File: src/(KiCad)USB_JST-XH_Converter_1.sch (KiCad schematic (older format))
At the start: 25 parts, among them SW1 SS-12D00G3, U2 TLP293

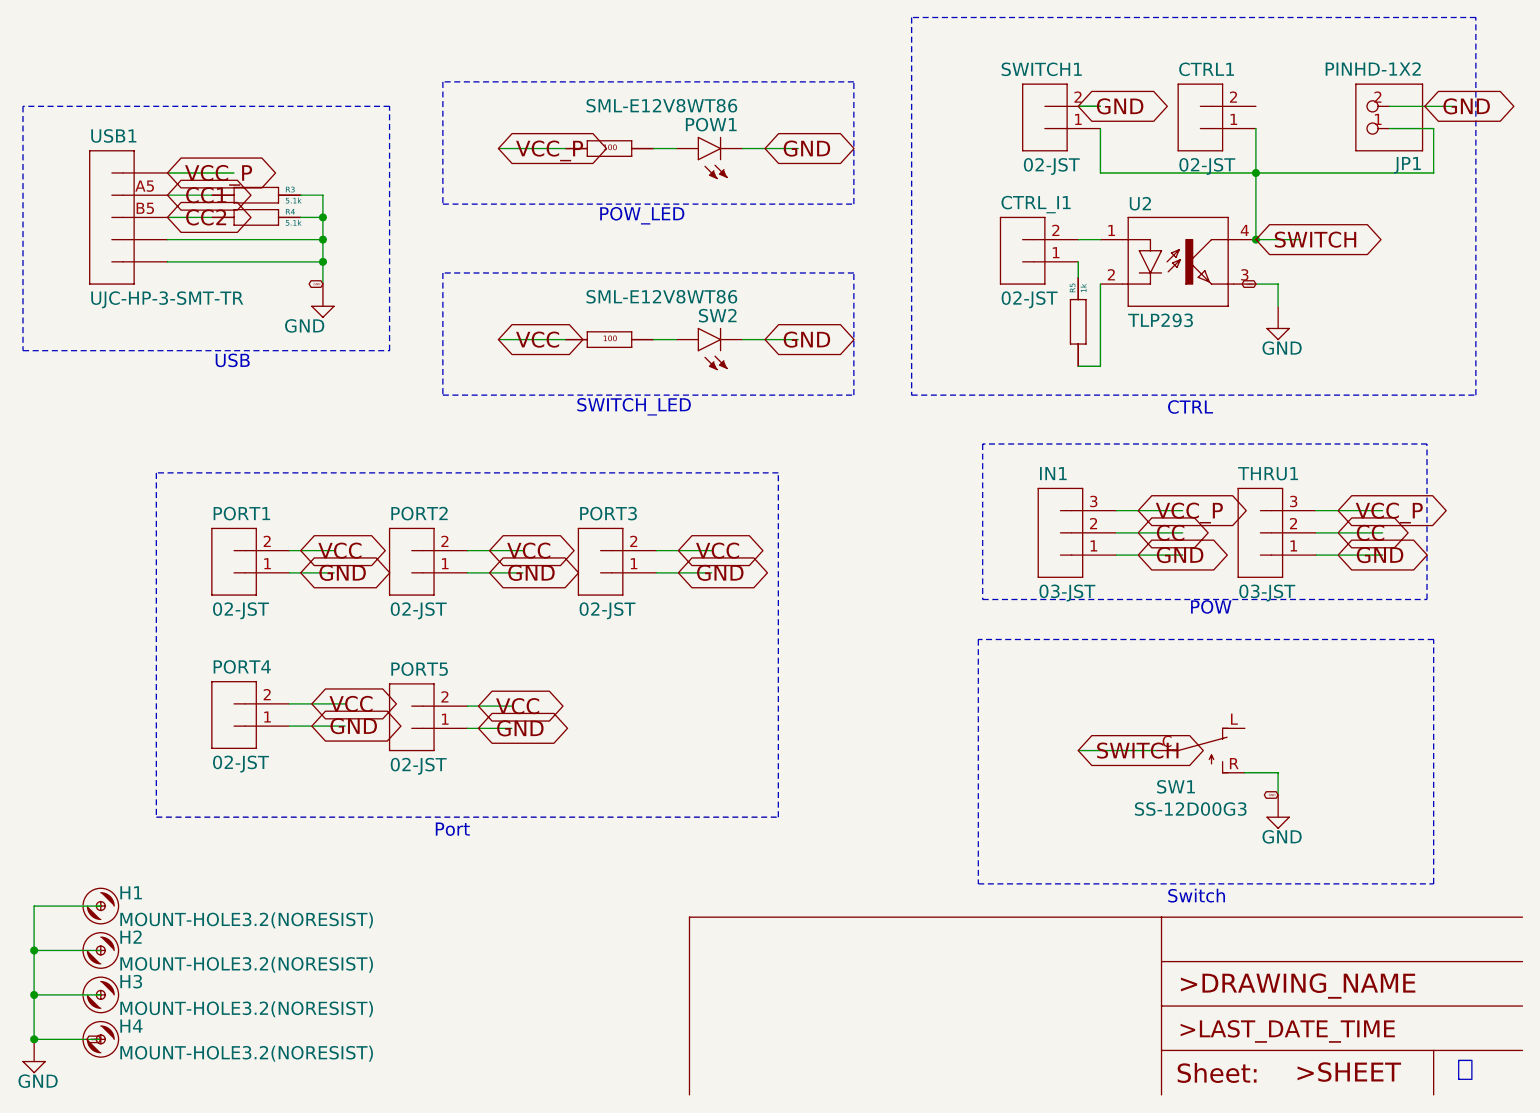
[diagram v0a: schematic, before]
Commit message: 3Aモード用LEDの追加
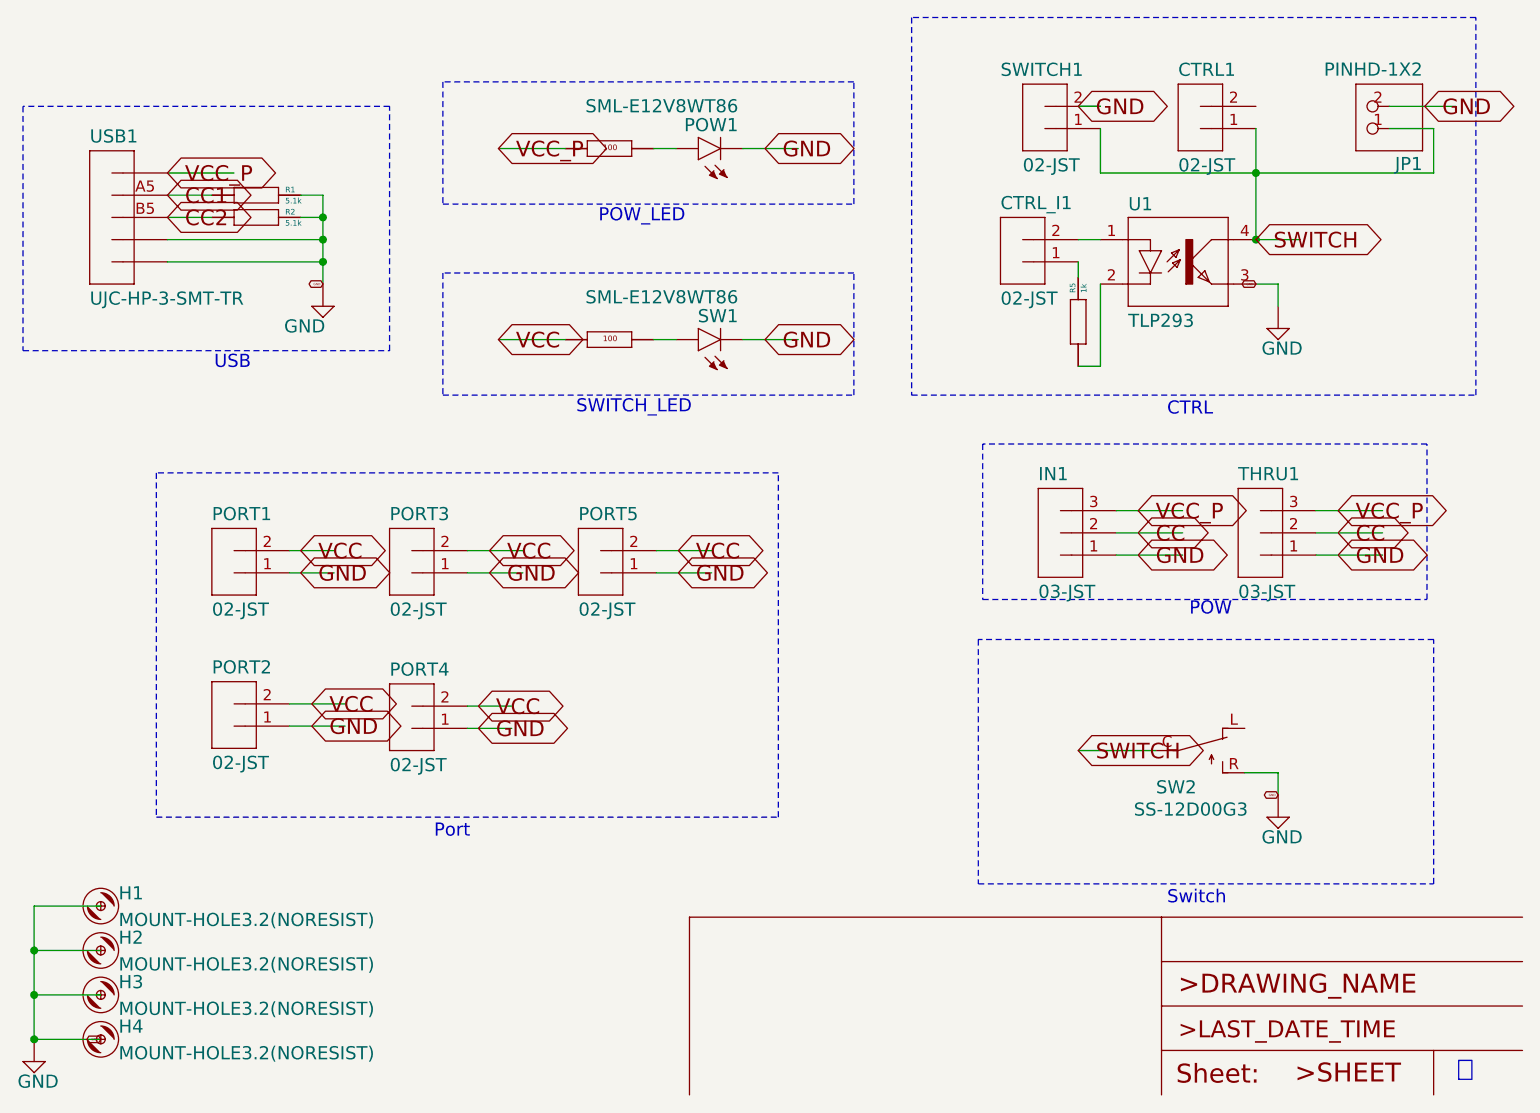
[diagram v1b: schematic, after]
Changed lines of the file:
@@
 AR Path="/CC96BE83" Ref="#FRAME1"  Part="1"
 AR Path="/639B4B9A/CC96BE83" Ref="#FRAME1"  Part="1"
+AR Path="/639EA9E5/CC96BE83" Ref="#FRAME1"  Part="1"
 F 0 "#FRAME1" H 2300 6600 50  0001 C CNN
 F 1 "A5L-LOC" H 2300 6600 50  0001 C CNN
@@
 AR Path="/96A0C2AF" Ref="PORT1"  Part="1"
 AR Path="/639B4B9A/96A0C2AF" Ref="PORT1"  Part="1"
+AR Path="/639EA9E5/96A0C2AF" Ref="PORT1"  Part="1"
 F 0 "PORT1" H 3500 4130 59  0000 L BNN
 F 1 "02-JST" H 3500 3700 59  0000 L BNN
@@
 AR Path="/DE65265B" Ref="PORT2"  Part="1"
 AR Path="/639B4B9A/DE65265B" Ref="PORT2"  Part="1"
-F 0 "PORT2" H 4300 4130 59  0000 L BNN
+AR Path="/639EA9E5/DE65265B" Ref="PORT3"  Part="1"
+F 0 "PORT3" H 4300 4130 59  0000 L BNN
 F 1 "02-JST" H 4300 3700 59  0000 L BNN
 F 2 "USB_JST-XH_Converter:B2B-XH" H 4350 4000 50  0001 C CNN
@@
 AR Path="/AF48B7E8" Ref="PORT3"  Part="1"
 AR Path="/639B4B9A/AF48B7E8" Ref="PORT3"  Part="1"
-F 0 "PORT3" H 5150 4130 59  0000 L BNN
+AR Path="/639EA9E5/AF48B7E8" Ref="PORT5"  Part="1"
+F 0 "PORT5" H 5150 4130 59  0000 L BNN
 F 1 "02-JST" H 5150 3700 59  0000 L BNN
 F 2 "USB_JST-XH_Converter:B2B-XH" H 5200 4000 50  0001 C CNN
@@
 AR Path="/423DE5BD" Ref="PORT4"  Part="1"
 AR Path="/639B4B9A/423DE5BD" Ref="PORT4"  Part="1"
-F 0 "PORT4" H 3500 4820 59  0000 L BNN
+AR Path="/639EA9E5/423DE5BD" Ref="PORT2"  Part="1"
+F 0 "PORT2" H 3500 4820 59  0000 L BNN
 F 1 "02-JST" H 3500 4390 59  0000 L BNN
 F 2 "USB_JST-XH_Converter:B2B-XH" H 3550 4690 50  0001 C CNN
@@
 AR Path="/35EB9426" Ref="PORT5"  Part="1"
 AR Path="/639B4B9A/35EB9426" Ref="PORT5"  Part="1"
-F 0 "PORT5" H 4300 4830 59  0000 L BNN
+AR Path="/639EA9E5/35EB9426" Ref="PORT4"  Part="1"
+F 0 "PORT4" H 4300 4830 59  0000 L BNN
 F 1 "02-JST" H 4300 4400 59  0000 L BNN
 F 2 "USB_JST-XH_Converter:B2B-XH" H 4350 4700 50  0001 C CNN
@@
 AR Path="/F85A3293" Ref="SW1"  Part="1"
 AR Path="/639B4B9A/F85A3293" Ref="SW1"  Part="1"
-F 0 "SW1" V 8150 4700 59  0000 L BNN
+AR Path="/639EA9E5/F85A3293" Ref="SW2"  Part="1"
+F 0 "SW2" V 8150 4700 59  0000 L BNN
 F 1 "SS-12D00G3" V 8250 4600 59  0000 L BNN
 F 2 "USB_JST-XH_Converter:SS-12D00G3" H 7950 4900 50  0001 C CNN
@@
 AR Path="/F54A36B8" Ref="#SUPPLY1"  Part="1"
 AR Path="/639B4B9A/F54A36B8" Ref="#SUPPLY01"  Part="1"
-F 0 "#SUPPLY01" H 8300 5200 50  0001 C CNN
+AR Path="/639EA9E5/F54A36B8" Ref="#SUPPLY0101"  Part="1"
+F 0 "#SUPPLY0101" H 8300 5200 50  0001 C CNN
 F 1 "GND" H 8225 5075 59  0000 L BNN
 F 2 "" H 8300 5200 50  0001 C CNN
@@
 AR Path="/5CC1AECC" Ref="SW"  Part="1"
 AR Path="/639B4B9A/5CC1AECC" Ref="SW2"  Part="1"
-F 0 "SW2" V 5830 2870 59  0000 L BNN
+AR Path="/639EA9E5/5CC1AECC" Ref="SW1"  Part="1"
+F 0 "SW1" V 5830 2870 59  0000 L BNN
 F 1 "SML-E12V8WT86" V 5915 2870 59  0000 L BNN
 F 2 "USB_JST-XH_Converter:SML-E12V8WT86" H 5690 3050 50  0001 C CNN
@@
 AR Path="/855FDFDB" Ref="R2"  Part="1"
 AR Path="/639B4B9A/855FDFDB" Ref="R2"  Part="1"
-F 0 "R2" H 5290 3050 50  0001 C CNN
+AR Path="/639EA9E5/855FDFDB" Ref="R4"  Part="1"
+F 0 "R4" H 5290 3050 50  0001 C CNN
 F 1 "RG2012N-101-B-T5" H 5290 3050 50  0001 C CNN
 F 2 "USB_JST-XH_Converter:RG2012" H 5290 3050 50  0001 C CNN
@@
 AR Path="/19032892" Ref="#SUPPLY2"  Part="1"
 AR Path="/639B4B9A/19032892" Ref="#SUPPLY02"  Part="1"
-F 0 "#SUPPLY02" H 2700 6300 50  0001 C CNN
+AR Path="/639EA9E5/19032892" Ref="#SUPPLY0102"  Part="1"
+F 0 "#SUPPLY0102" H 2700 6300 50  0001 C CNN
 F 1 "GND" H 2625 6175 59  0000 L BNN
 F 2 "" H 2700 6300 50  0001 C CNN
@@
 AR Path="/9910BFD8" Ref="H1"  Part="1"
 AR Path="/639B4B9A/9910BFD8" Ref="H1"  Part="1"
+AR Path="/639EA9E5/9910BFD8" Ref="H1"  Part="1"
 F 0 "H1" H 3080 5623 59  0000 L BNN
 F 1 "MOUNT-HOLE3.2(NORESIST)" H 3080 5503 59  0000 L BNN
@@
 AR Path="/5D268E00" Ref="H2"  Part="1"
 AR Path="/639B4B9A/5D268E00" Ref="H2"  Part="1"
+AR Path="/639EA9E5/5D268E00" Ref="H2"  Part="1"
 F 0 "H2" H 3080 5823 59  0000 L BNN
 F 1 "MOUNT-HOLE3.2(NORESIST)" H 3080 5703 59  0000 L BNN
@@
 AR Path="/DE67D20D" Ref="H3"  Part="1"
 AR Path="/639B4B9A/DE67D20D" Ref="H3"  Part="1"
+AR Path="/639EA9E5/DE67D20D" Ref="H3"  Part="1"
 F 0 "H3" H 3080 6023 59  0000 L BNN
 F 1 "MOUNT-HOLE3.2(NORESIST)" H 3080 5903 59  0000 L BNN
@@
 AR Path="/EA162BAB" Ref="H4"  Part="1"
 AR Path="/639B4B9A/EA162BAB" Ref="H4"  Part="1"
+AR Path="/639EA9E5/EA162BAB" Ref="H4"  Part="1"
 F 0 "H4" H 3080 6223 59  0000 L BNN
 F 1 "MOUNT-HOLE3.2(NORESIST)" H 3080 6103 59  0000 L BNN
@@
 AR Path="/4F8E092B" Ref="#SUPPLY3"  Part="1"
 AR Path="/639B4B9A/4F8E092B" Ref="#SUPPLY03"  Part="1"
-F 0 "#SUPPLY03" H 4000 2900 50  0001 C CNN
+AR Path="/639EA9E5/4F8E092B" Ref="#SUPPLY0103"  Part="1"
+F 0 "#SUPPLY0103" H 4000 2900 50  0001 C CNN
 F 1 "GND" H 3825 2775 59  0000 L BNN
 F 2 "" H 4000 2900 50  0001 C CNN
@@
 AR Path="/9A4BB1DE" Ref="R3"  Part="1"
 AR Path="/639B4B9A/9A4BB1DE" Ref="R3"  Part="1"
-F 0 "R3" H 3830 2410 25  0000 L BNN
+AR Path="/639EA9E5/9A4BB1DE" Ref="R1"  Part="1"
+F 0 "R1" H 3830 2410 25  0000 L BNN
 F 1 "5.1k" H 3830 2360 25  0000 L BNN
 F 2 "USB_JST-XH_Converter:RG2012" H 3700 2400 50  0001 C CNN
@@
 AR Path="/80DF3A02" Ref="R4"  Part="1"
 AR Path="/639B4B9A/80DF3A02" Ref="R4"  Part="1"
-F 0 "R4" H 3830 2510 25  0000 L BNN
+AR Path="/639EA9E5/80DF3A02" Ref="R2"  Part="1"
+F 0 "R2" H 3830 2510 25  0000 L BNN
 F 1 "5.1k" H 3830 2460 25  0000 L BNN
 F 2 "USB_JST-XH_Converter:RG2012" H 3700 2500 50  0001 C CNN
@@
 AR Path="/BF4A4BA7" Ref="SWITCH"  Part="1"
 AR Path="/639B4B9A/BF4A4BA7" Ref="SWITCH1"  Part="1"
+AR Path="/639EA9E5/BF4A4BA7" Ref="SWITCH1"  Part="1"
 F 0 "SWITCH1" H 7050 2130 59  0000 L BNN
 F 1 "02-JST" H 7150 1700 59  0000 L BNN
@@
 AR Path="/E88FF595" Ref="CTRL"  Part="1"
 AR Path="/639B4B9A/E88FF595" Ref="CTRL1"  Part="1"
+AR Path="/639EA9E5/E88FF595" Ref="CTRL1"  Part="1"
 F 0 "CTRL1" H 7850 2130 59  0000 L BNN
 F 1 "02-JST" H 7850 1700 59  0000 L BNN
@@
 AR Path="/274AF3D0" Ref="CTRL_I"  Part="1"
 AR Path="/639B4B9A/274AF3D0" Ref="CTRL_I1"  Part="1"
+AR Path="/639EA9E5/274AF3D0" Ref="CTRL_I1"  Part="1"
 F 0 "CTRL_I1" H 7050 2730 59  0000 L BNN
 F 1 "02-JST" H 7050 2300 59  0000 L BNN
@@
 AR Path="/1C9152C2" Ref="#SUPPLY4"  Part="1"
 AR Path="/639B4B9A/1C9152C2" Ref="#SUPPLY04"  Part="1"
-F 0 "#SUPPLY04" H 8300 3000 50  0001 C CNN
+AR Path="/639EA9E5/1C9152C2" Ref="#SUPPLY0104"  Part="1"
+F 0 "#SUPPLY0104" H 8300 3000 50  0001 C CNN
 F 1 "GND" H 8225 2875 59  0000 L BNN
 F 2 "" H 8300 3000 50  0001 C CNN
@@
 AR Path="/4E0AB7A9" Ref="U2"  Part="1"
 AR Path="/639B4B9A/4E0AB7A9" Ref="U2"  Part="1"
-F 0 "U2" H 7625 2925 59  0000 L BNN
+AR Path="/639EA9E5/4E0AB7A9" Ref="U1"  Part="1"
+F 0 "U1" H 7625 2925 59  0000 L BNN
 F 1 "TLP293" H 7625 2400 59  0000 L BNN
 F 2 "USB_JST-XH_Converter:SO4_TOS" H 7900 2700 50  0001 C CNN
@@
 AR Path="/4373A00B" Ref="R5"  Part="1"
 AR Path="/639B4B9A/4373A00B" Ref="R5"  Part="1"
+AR Path="/639EA9E5/4373A00B" Ref="R5"  Part="1"
 F 0 "R5" H 7530 2980 25  0000 L BNN
 F 1 "1k" H 7530 2930 25  0000 L BNN
@@
 AR Path="/0B60073D" Ref="JP1"  Part="1"
 AR Path="/639B4B9A/0B60073D" Ref="JP1"  Part="1"
+AR Path="/639EA9E5/0B60073D" Ref="JP1"  Part="1"
 F 0 "JP1" H 8450 2225 59  0000 L BNN
 F 1 "PINHD-1X2" H 8450 1800 59  0000 L BNN
@@
 AR Path="/8264F283" Ref="POW"  Part="1"
 AR Path="/639B4B9A/8264F283" Ref="POW1"  Part="1"
+AR Path="/639EA9E5/8264F283" Ref="POW1"  Part="1"
 F 0 "POW1" V 5830 2010 59  0000 L BNN
 F 1 "SML-E12V8WT86" V 5915 2010 59  0000 L BNN
@@
 AR Path="/54673866" Ref="R1"  Part="1"
 AR Path="/639B4B9A/54673866" Ref="R1"  Part="1"
-F 0 "R1" H 5290 2190 50  0001 C CNN
+AR Path="/639EA9E5/54673866" Ref="R3"  Part="1"
+F 0 "R3" H 5290 2190 50  0001 C CNN
 F 1 "RG2012N-101-B-T5" H 5290 2190 50  0001 C CNN
 F 2 "USB_JST-XH_Converter:RG2012" H 5290 2190 50  0001 C CNN
@@
 AR Path="/CB343537" Ref="IN"  Part="1"
 AR Path="/639B4B9A/CB343537" Ref="IN1"  Part="1"
+AR Path="/639EA9E5/CB343537" Ref="IN1"  Part="1"
 F 0 "IN1" H 7220 4150 59  0000 L BNN
 F 1 "03-JST" H 7220 3620 59  0000 L BNN
@@
 AR Path="/BE8514DD" Ref="THRU"  Part="1"
 AR Path="/639B4B9A/BE8514DD" Ref="THRU1"  Part="1"
+AR Path="/639EA9E5/BE8514DD" Ref="THRU1"  Part="1"
 F 0 "THRU1" H 8120 4150 59  0000 L BNN
 F 1 "03-JST" H 8120 3620 59  0000 L BNN
@@
 AR Path="/022A0DE2" Ref="USB1"  Part="1"
 AR Path="/639B4B9A/022A0DE2" Ref="USB1"  Part="1"
+AR Path="/639EA9E5/022A0DE2" Ref="USB1"  Part="1"
 F 0 "USB1" H 2950 2830 59  0000 L BNN
 F 1 "UJC-HP-3-SMT-TR" H 2950 2100 59  0000 L BNN
